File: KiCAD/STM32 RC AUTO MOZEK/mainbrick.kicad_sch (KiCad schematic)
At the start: 40 parts, among them J8 Conn_01x05_Socket, U10 ACS712xLCTR-20A, U11 ACS712xLCTR-20A, U13 STM32F030C8Tx, U14 BME280, U4 ACS712xLCTR-20A, U5 NRF24L01_Breakout, U7 ACS712xLCTR-20A, U8 ACS712xLCTR-20A, U9 ACS712xLCTR-20A, Y1 32.786KHz, Y2 25MHz

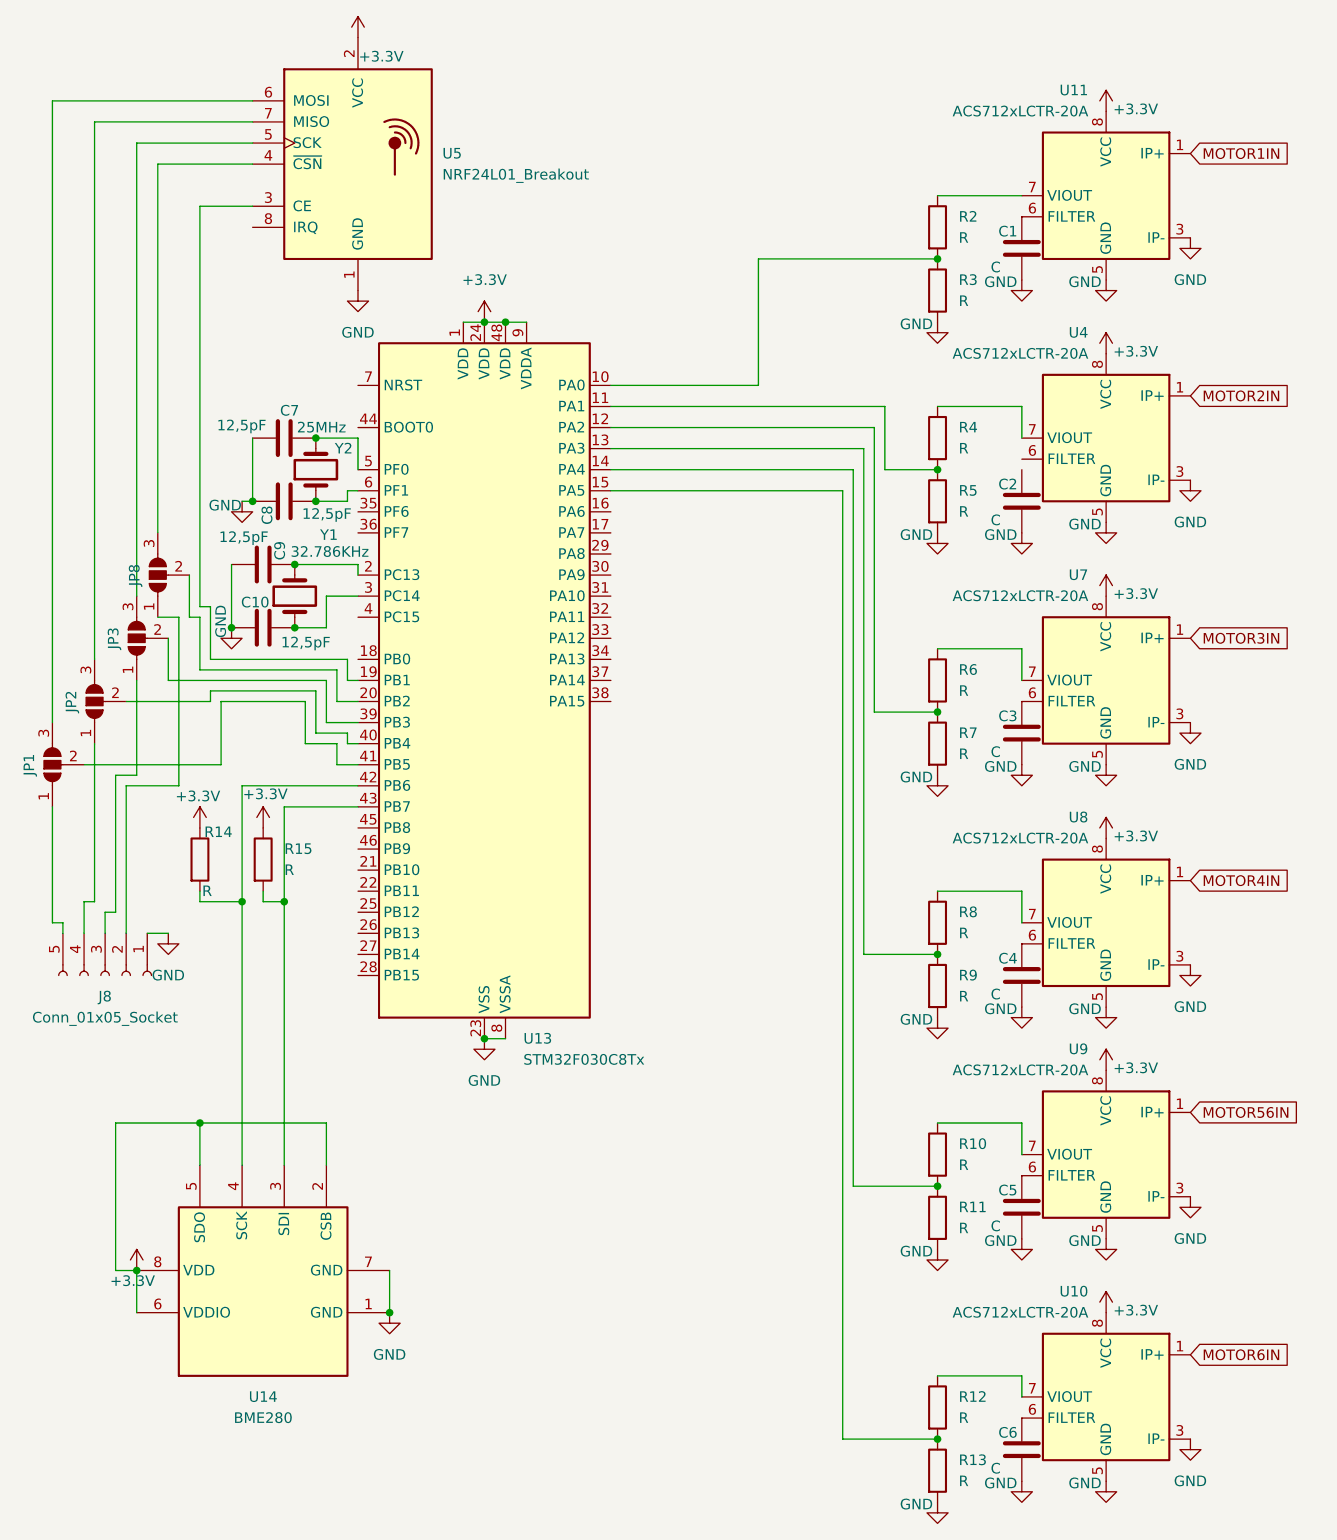
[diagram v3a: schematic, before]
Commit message: adding completation on schematic, working on board
need to add SWD Debug as input for programing
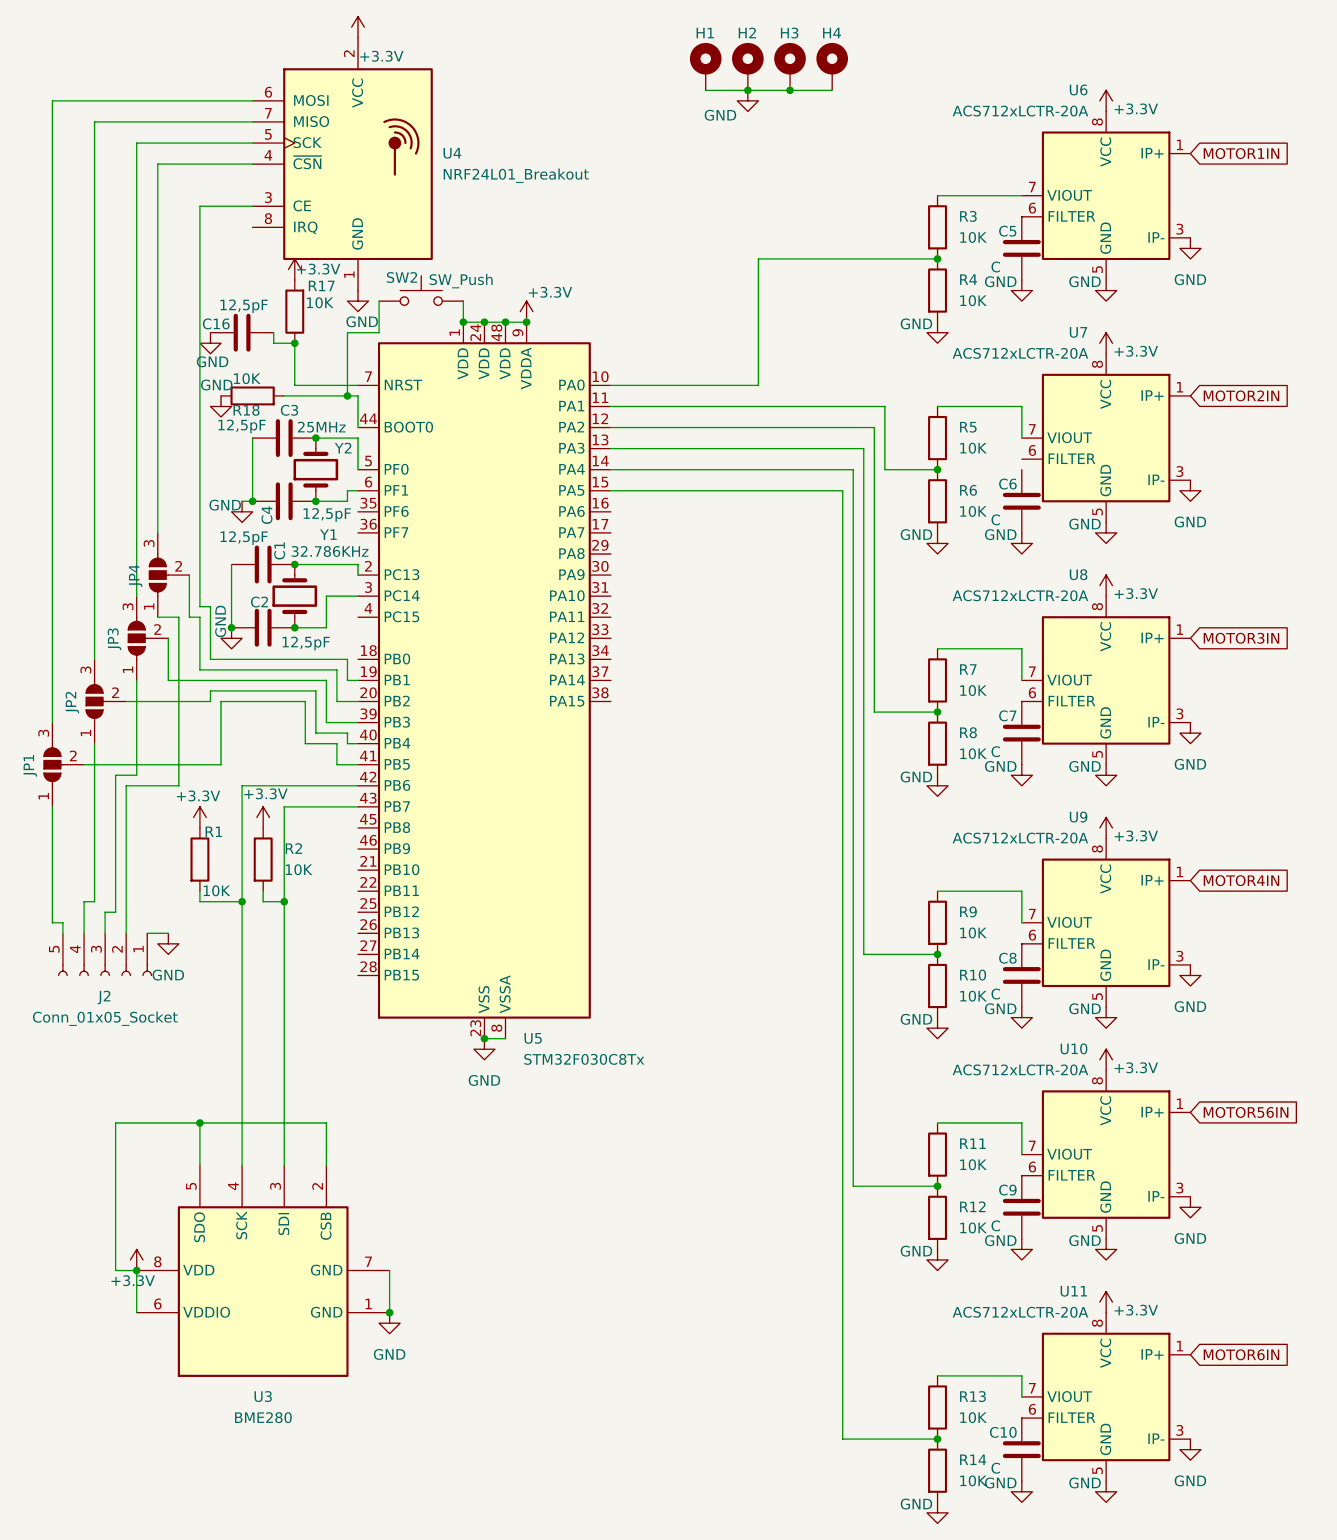
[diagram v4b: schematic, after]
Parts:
- removed R3: R, Resistor_SMD:R_0805_2012Metric_Pad1.20x1.40mm_HandSolder, symbol Device:R
- added C16: 12,5pF, Capacitor_SMD:C_0805_2012Metric_Pad1.18x1.45mm_HandSolder, symbol Device:C
- added H1, H2, H3, H4: MountingHole_Pad, MountingHole:MountingHole_3.5mm_Pad_Via, symbol Mechanical:MountingHole_Pad
- added R14, R17, R18: 10K, Resistor_SMD:R_0805_2012Metric_Pad1.20x1.40mm_HandSolder, symbol Device:R
- added SW2: SW_Push, Button_Switch_SMD:SW_SPST_CK_RS282G05A3, symbol Switch:SW_Push
- R1: renamed from R14; value R -> 10K
- R10, R11, R12, R13, R4, R5, R6, R7, R8, R9: value R -> 10K
- R2: renamed from R15; value R -> 10K
- R3: renamed from R2; value R -> 10K
- renumbered C9 to C1, C6 to C10, C10 to C2, C7 to C3, C8 to C4, C1 to C5, C2 to C6, C3 to C7, C4 to C8, C5 to C9, J8 to J2, JP8 to JP4, U9 to U10, U10 to U11, U14 to U3, U5 to U4, U13 to U5, U11 to U6, U4 to U7, U7 to U8, U8 to U9
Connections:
- net +3.3V: now also R17.2, SW2.2
- net GND: now also R10.2, R12.2, R4.2, R6.2, R8.2, C16.2, H1.1, H2.1, H3.1, H4.1, R14.2, R18.1; no longer R11.2, R13.2, R5.2, R7.2, R9.2
- net at R12.1: now also R11.2, U5.14 (PA4); no longer U11.7 (VIOUT)
- net at U9.7 (VIOUT): now also R9.1; no longer R8.1
- net at U7.7 (VIOUT): now also R5.1; no longer R4.1
- net at R10.1: now also R9.2, U5.13 (PA3); no longer U10.7 (VIOUT)
- net at R3.2, U5.10 (PA0): now also R4.1
- net at R6.1: now also R5.2, U5.11 (PA1); no longer U8.7 (VIOUT)
- net at U5.44 (BOOT0): now also R18.2, SW2.1
- net at U5.7 (NRST): now also C16.1, R17.1
- new net: R13.2, R14.1, U5.15 (PA5)
- new net: R11.1, U10.7 (VIOUT)
- new net: R13.1, U11.7 (VIOUT)
- new net: R7.2, R8.1, U5.12 (PA2)
- new net: R7.1, U8.7 (VIOUT)

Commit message: .
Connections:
- net +3.3V: no longer U10.8 (VCC), U11.8 (VCC), U6.8 (VCC), U7.8 (VCC), U8.8 (VCC), U9.8 (VCC)
- net at C6.1: now also U7.6 (FILTER)
- net MOTOR56IN renamed MOTOR5IN
- new net +5V: U10.8 (VCC), U11.8 (VCC), U6.8 (VCC), U7.8 (VCC), U8.8 (VCC), U9.8 (VCC)
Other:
- moved on the sheet: C6
